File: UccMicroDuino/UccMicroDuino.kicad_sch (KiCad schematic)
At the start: 14 parts, among them J1 Pcb USB type A, J2 Header, U1 ATtiny85-20S

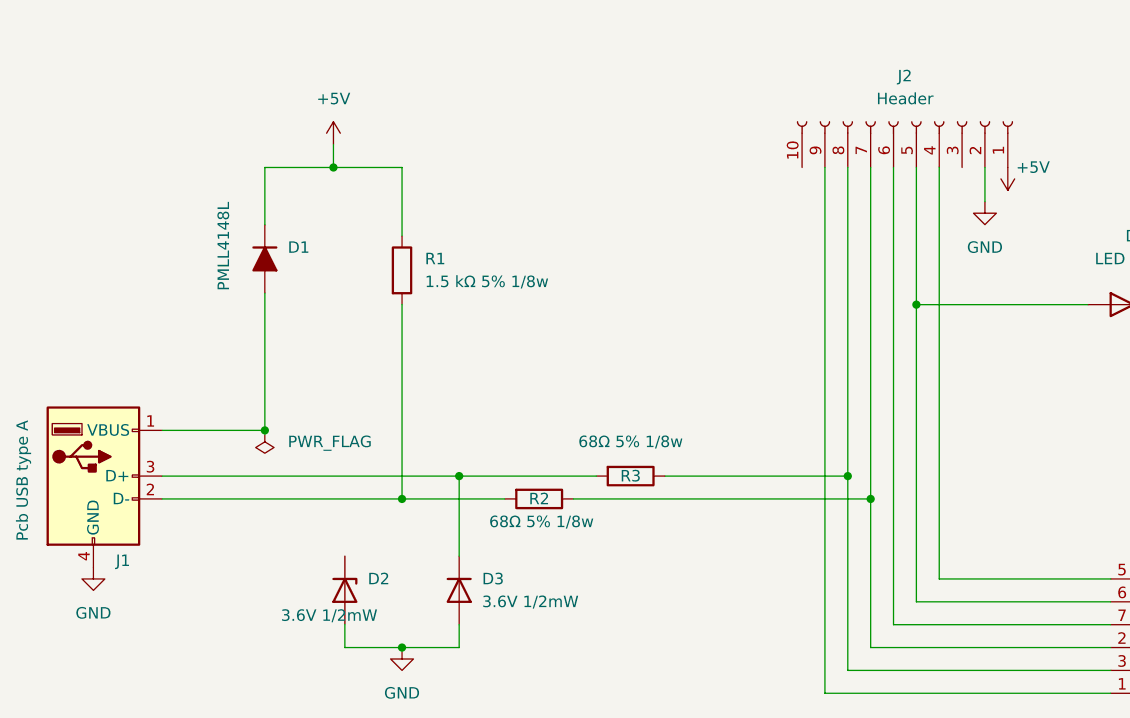
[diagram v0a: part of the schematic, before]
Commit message: Esquematico principal terminado
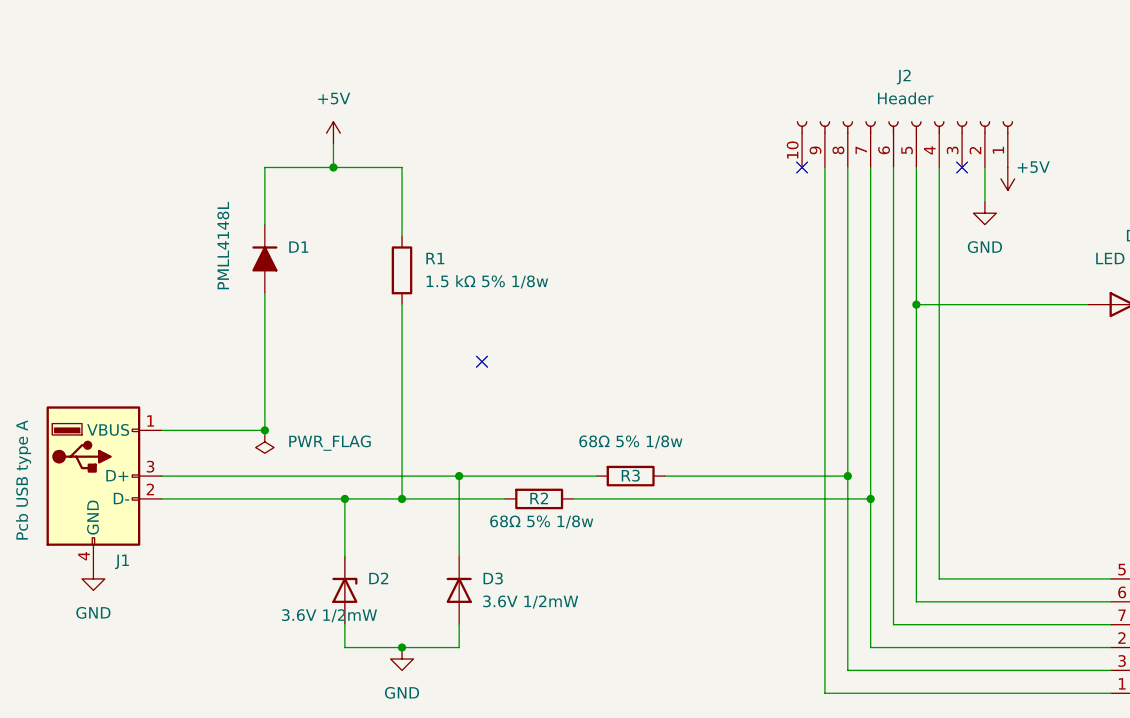
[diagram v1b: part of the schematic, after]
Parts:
- D3: footprint (none) -> Diode_SMD:D_SOD-123
- D4: footprint (none) -> ledSmd:ledSMD
- R2, R3, R4, R5: footprint (none) -> Resistor_SMD:R_0805_2012Metric_Pad1.20x1.40mm_HandSolder
- U1: footprint Package_SO:SOIC-8W_5.3x5.3mm_P1.27mm -> Package_SO:SOIC-8_5.3x5.3mm_P1.27mm
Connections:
- net at J1.2 (D-), R1.2, R2.2: now also D2.1 (K)
- no-connect marks 0 -> 3
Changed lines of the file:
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@@
+	)
+	(junction
+		(at 85.09 104.14)
+		(diameter 0)
+		(color 0 0 0 0)
 	)
 	(junction
@@
 		(color 0 0 0 0)
 	)
+	(no_connect
+		(at 135.89 67.31)
+	)
+	(no_connect
+		(at 100.33 88.9)
+	)
+	(no_connect
+		(at 153.67 67.31)
+	)
 	(wire
 		(pts
@@
 	(wire
 		(pts
+			(xy 85.09 104.14) (xy 91.44 104.14)
+		)
+		(stroke
+			(width 0)
+			(type default)
+		)
+	)
+	(wire
+		(pts
 			(xy 156.21 67.31) (xy 156.21 71.12)
 		)
@@
 	(wire
 		(pts
+			(xy 85.09 104.14) (xy 85.09 110.49)
+		)
+		(stroke
+			(width 0)
+			(type default)
+		)
+	)
+	(wire
+		(pts
 			(xy 91.44 67.31) (xy 83.82 67.31)
 		)
@@
 	(wire
 		(pts
-			(xy 64.77 104.14) (xy 91.44 104.14)
+			(xy 64.77 104.14) (xy 85.09 104.14)
 		)
 		(stroke
@@
 			)
 		)
-		(property "Footprint" "Package_SO:SOIC-8W_5.3x5.3mm_P1.27mm"
+		(property "Footprint" "Package_SO:SOIC-8_5.3x5.3mm_P1.27mm"
 			(at 185.42 120.65 0)
 			(hide yes)
@@
 			)
 		)
-		(property "Footprint" ""
+		(property "Footprint" "Resistor_SMD:R_0805_2012Metric_Pad1.20x1.40mm_HandSolder"
 			(at 259.588 88.9 90)
 			(hide yes)
@@
 			)
 		)
-		(property "Footprint" ""
+		(property "Footprint" "Resistor_SMD:R_0805_2012Metric_Pad1.20x1.40mm_HandSolder"
 			(at 185.42 80.772 90)
 			(hide yes)
@@
 			)
 		)
-		(property "Footprint" ""
+		(property "Footprint" "Diode_SMD:D_SOD-123"
 			(at 97.79 114.3 0)
 			(hide yes)
@@
 			)
 		)
-		(property "Footprint" ""
+		(property "Footprint" "ledSmd:ledSMD"
 			(at 171.45 82.55 0)
 			(hide yes)
@@
 			)
 		)
-		(property "Footprint" ""
+		(property "Footprint" "Resistor_SMD:R_0805_2012Metric_Pad1.20x1.40mm_HandSolder"
 			(at 116.84 99.822 90)
 			(hide yes)
@@
 			)
 		)
-		(property "Footprint" ""
+		(property "Footprint" "Resistor_SMD:R_0805_2012Metric_Pad1.20x1.40mm_HandSolder"
 			(at 106.68 102.362 90)
 			(hide yes)
